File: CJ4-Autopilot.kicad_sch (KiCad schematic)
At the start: 41 parts

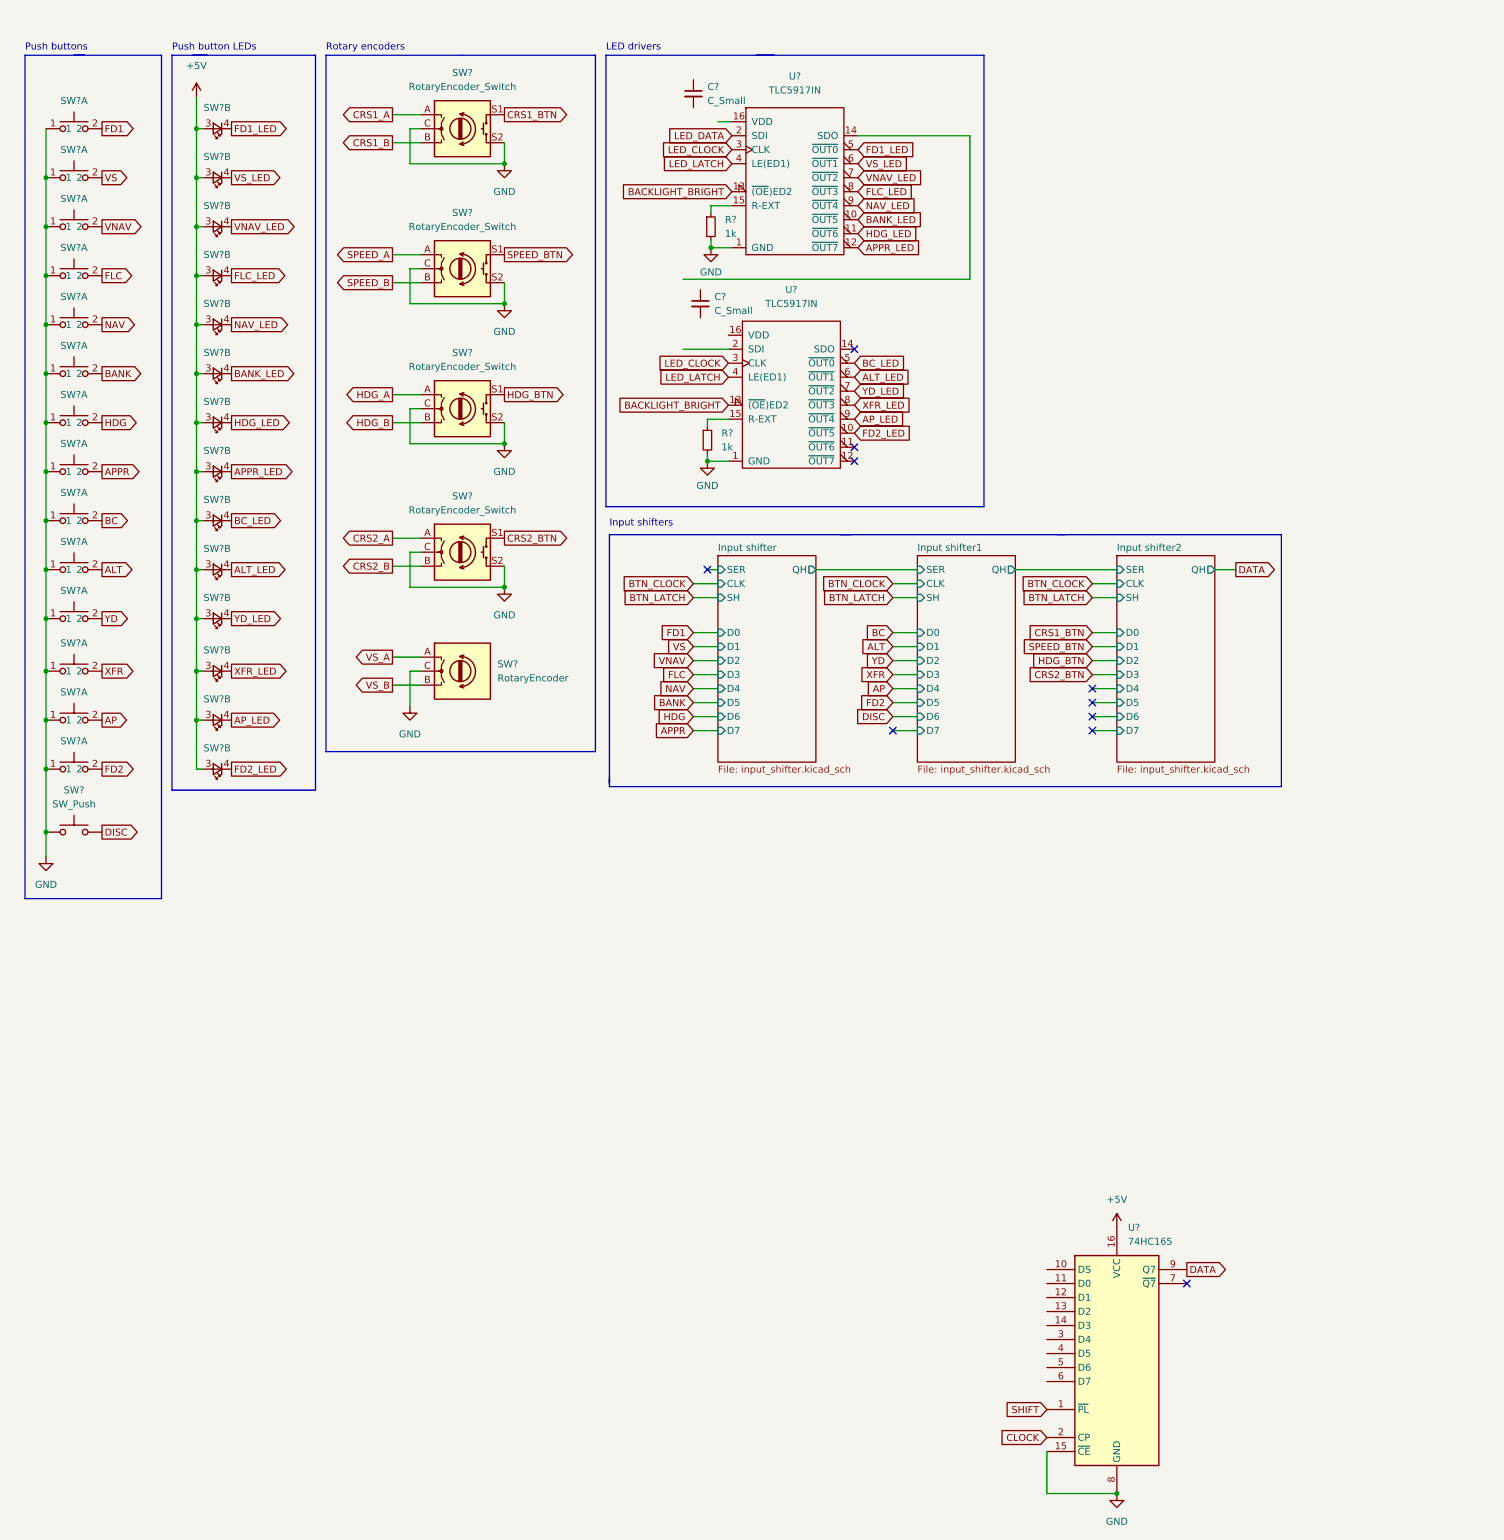
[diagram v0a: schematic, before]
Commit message: Added pico
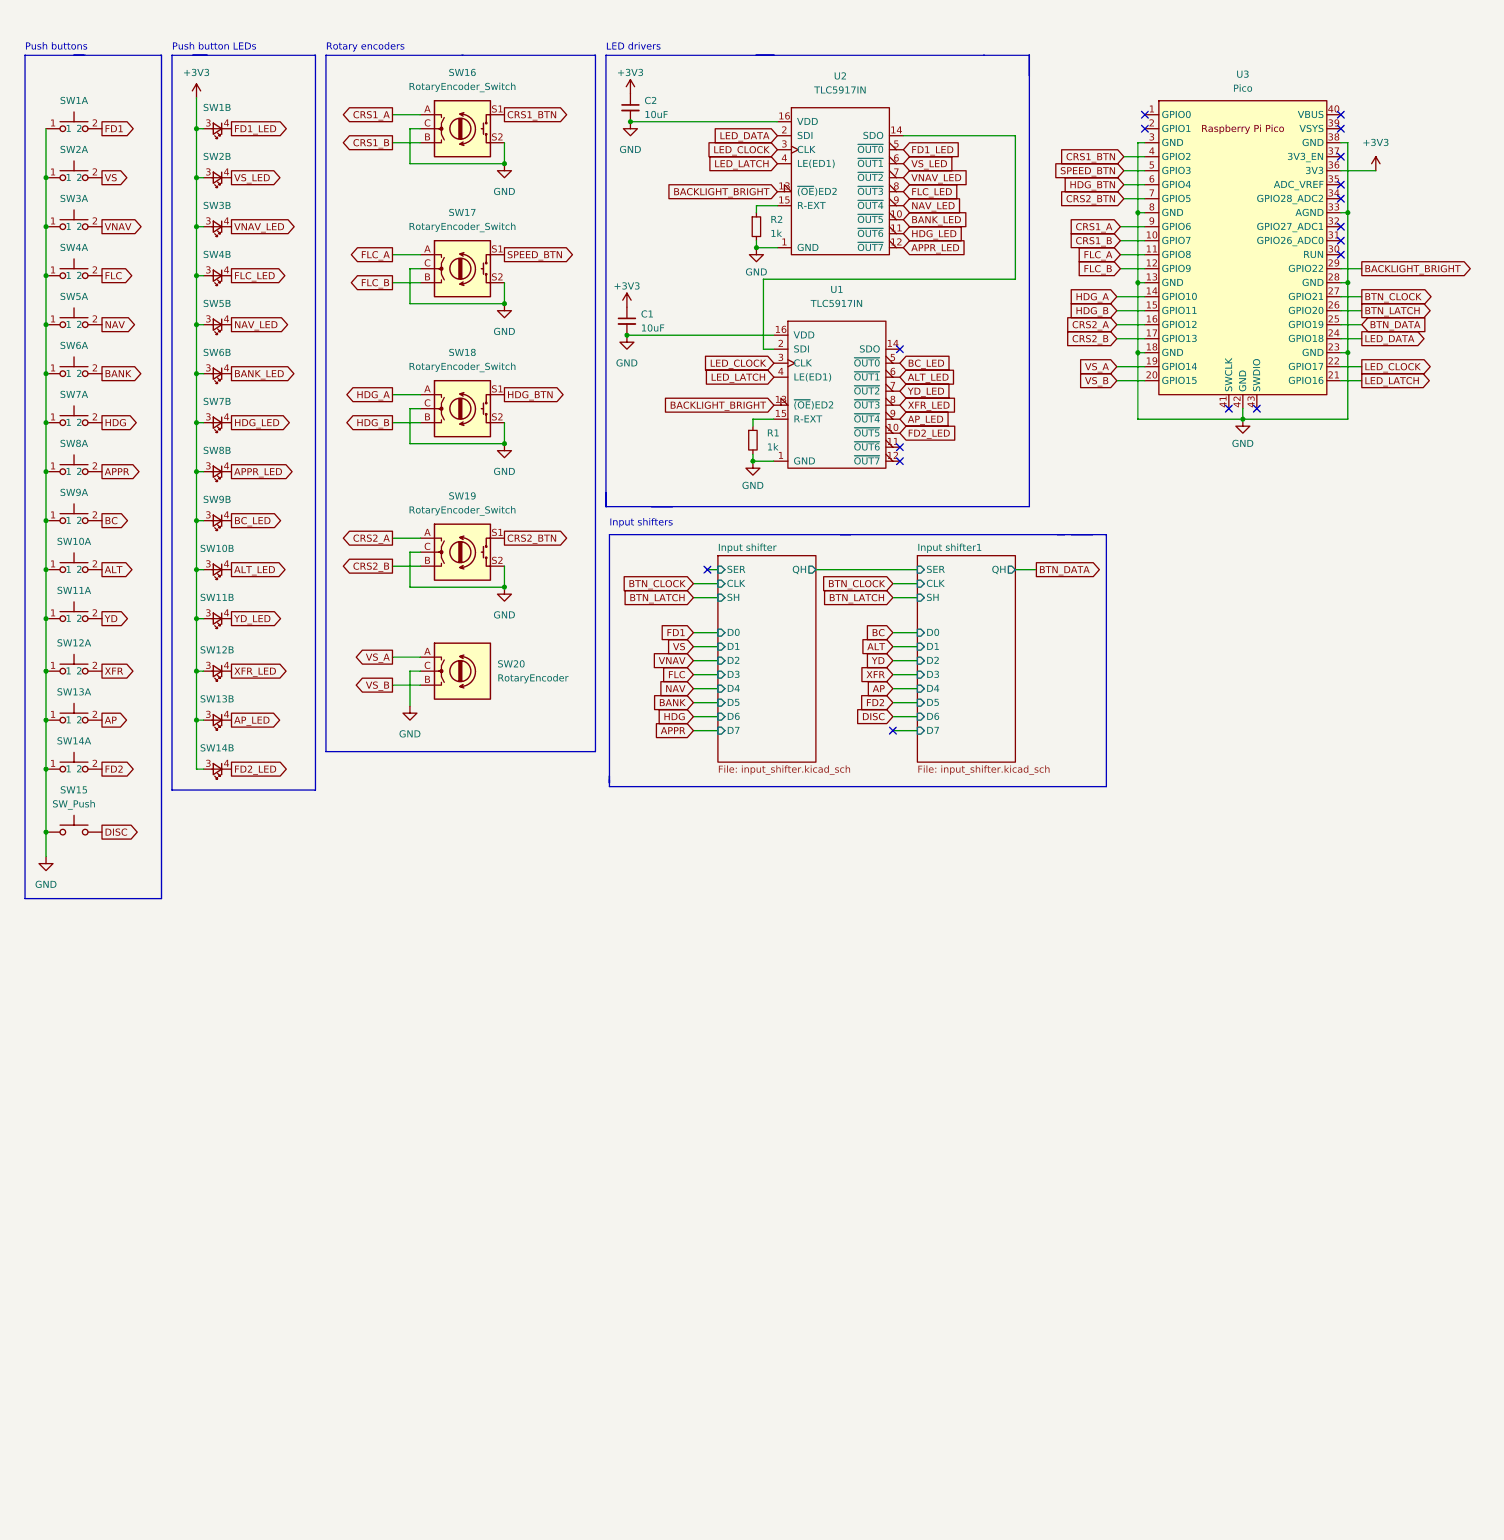
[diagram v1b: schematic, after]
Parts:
- removed C? (x2): C_Small, symbol Device:C_Small
- removed U?: 74HC165, symbol 74xx:74HC165
- added C1, C2: 10uF, symbol Device:C_Small
- added U3: Pico, RPi_Pico:RPi_Pico_SMD_TH, symbol MCU_RaspberryPi_and_Boards:Pico
- gave numbers to parts that had none: 24
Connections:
- net BACKLIGHT_BRIGHT: now also U3.29 (GPIO22)
- net BTN_CLOCK: now also U3.27 (GPIO21)
- net BTN_LATCH: now also U3.26 (GPIO20)
- net CRS1_A: now also U3.9 (GPIO6)
- net CRS1_B: now also U3.10 (GPIO7)
- net CRS1_BTN: now also U3.4 (GPIO2)
- net CRS2_A: now also U3.16 (GPIO12)
- net CRS2_B: now also U3.17 (GPIO13)
- net CRS2_BTN: now also U3.7 (GPIO5)
- net GND: now also U1.16 (VDD), U2.16 (VDD), C1.2, C2.2, U3.13 (GND), U3.18 (GND), U3.23 (GND), U3.28 (GND), U3.3 (GND), U3.33 (AGND), U3.38 (GND), U3.42 (GND), U3.8 (GND)
- net HDG_A: now also U3.14 (GPIO10)
- net HDG_B: now also U3.15 (GPIO11)
- net HDG_BTN: now also U3.6 (GPIO4)
- net LED_CLOCK: now also U3.22 (GPIO17)
- net LED_DATA: now also U3.24 (GPIO18)
- net LED_LATCH: now also U3.21 (GPIO16)
- net SPEED_BTN: now also U3.5 (GPIO3)
- net VS_A: now also U3.19 (GPIO14)
- net VS_B: now also U3.20 (GPIO15)
- net at U1.2 (SDI): now also U2.14 (SDO)
- net +5V renamed +3V3
- net +3V3: now also C1.1, C2.1, U3.36 (3V3)
- net SPEED_A renamed FLC_A
- net FLC_A: now also U3.11 (GPIO8)
- net SPEED_B renamed FLC_B
- net FLC_B: now also U3.12 (GPIO9)
- new net BTN_DATA: U3.25 (GPIO19)
- no-connect marks 10 -> 17
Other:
- removed sheet Input shifter2
- moved on the sheet: R1, R2, U1, U2

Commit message: Full schematic done
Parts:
- removed SW16, SW17, SW18, SW19: RotaryEncoder_Switch, symbol Device:RotaryEncoder_Switch
- removed SW20: RotaryEncoder, symbol Device:RotaryEncoder
- added H1, H10, H11, H2, H3, H4, H9: MountingHole, MountingHole:MountingHole_3.2mm_M3, symbol Mechanical:MountingHole
- added H5, H6, H7, H8: MountingHole, CJ4-Autopilot:MountingHole_7.5mm, symbol Mechanical:MountingHole
- added J1, J2, J3, J4: Conn_01x05, CJ4-Autopilot:SW_PUSH_6mm, symbol Connector_Generic:Conn_01x05
- added SW16: RotaryEncoder, CJ4-Autopilot:EN11-VNB1BQ15, symbol Device:RotaryEncoder
- C1: renamed from C2; footprint (none) -> Capacitor_SMD:C_0603_1608Metric
- C2: renamed from C1; footprint (none) -> Capacitor_SMD:C_0603_1608Metric
- R1: renamed from R2; footprint (none) -> CJ4-Autopilot:SW_PUSH_6mm; JLC (none) -> 0603; LCSC (none) -> C21190
- R2: renamed from R1; footprint (none) -> CJ4-Autopilot:SW_PUSH_6mm; JLC (none) -> 0603; LCSC (none) -> C21190
- SW1, SW10, SW11, SW12, SW13, SW14, SW2, SW3, SW4, SW5, SW6, SW7, SW8, SW9: footprint (none) -> CJ4-Autopilot:SW_PUSH_6mm
- SW15: footprint (none) -> Button_Switch_THT:SW_PUSH_6mm
- U2: renamed from U3; footprint RPi_Pico:RPi_Pico_SMD_TH -> MCU_RaspberryPi_and_Boards:RPi_Pico_SMD_TH
- renumbered U2 to U1, U1 to U3
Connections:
- net +3V3: no longer SW1.3, SW10.3, SW11.3, SW12.3, SW13.3, SW14.3, SW2.3, SW3.3, SW4.3, SW5.3, SW6.3, SW7.3, SW8.3, SW9.3
- net CRS1_A: now also J1.1 (Pin_1)
- net CRS1_B: now also J1.3 (Pin_3)
- net CRS1_BTN: now also J1.4 (Pin_4)
- net CRS2_A: now also J4.1 (Pin_1)
- net CRS2_B: now also J4.3 (Pin_3)
- net CRS2_BTN: now also J4.4 (Pin_4)
- net FLC_A: now also J2.1 (Pin_1)
- net FLC_B: now also J2.3 (Pin_3)
- net GND: now also J1.2 (Pin_2), J1.5 (Pin_5), J2.2 (Pin_2), J2.5 (Pin_5), J3.2 (Pin_2), J3.5 (Pin_5), J4.2 (Pin_2), J4.5 (Pin_5), SW16.C
- net HDG_A: now also J3.1 (Pin_1)
- net HDG_B: now also J3.3 (Pin_3)
- net HDG_BTN: now also J3.4 (Pin_4)
- net SPEED_BTN: now also J2.4 (Pin_4)
- net VS_A: now also SW16.A
- net VS_B: now also SW16.B
- net +5V: now reaches U2.40 (VBUS)
- net +5V: now also SW1.3, SW10.3, SW11.3, SW12.3, SW13.3, SW14.3, SW2.3, SW3.3, SW4.3, SW5.3, SW6.3, SW7.3, SW8.3, SW9.3
- no-connect marks 17 -> 16
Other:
- note added: "Board mounting"
- note added: "Encoder mounting"
- note added: "JLCPCB tooling"
- note added: "Mounting holes"
- note added: "Raspberry Pi Pico"
- title: (none) -> CJ4 Autopilot Panel
- moved on the sheet: C1, C2, R1, R2, SW10A, SW10B, SW11A, SW11B, SW12A, SW12B, SW13A, SW13B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
